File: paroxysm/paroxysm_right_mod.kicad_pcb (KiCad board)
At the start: 2 copper layers, 117.5 x 89.9 mm, 20 parts, among them SW10 SW_Push, SW11 SW_Push, SW12 SW_Push, SW14 SW_Push, SW15 SW_Push, SW16 SW_Push, SW17 SW_Push, SW18 SW_Push, SW20 SW_Push, SW21 SW_Push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

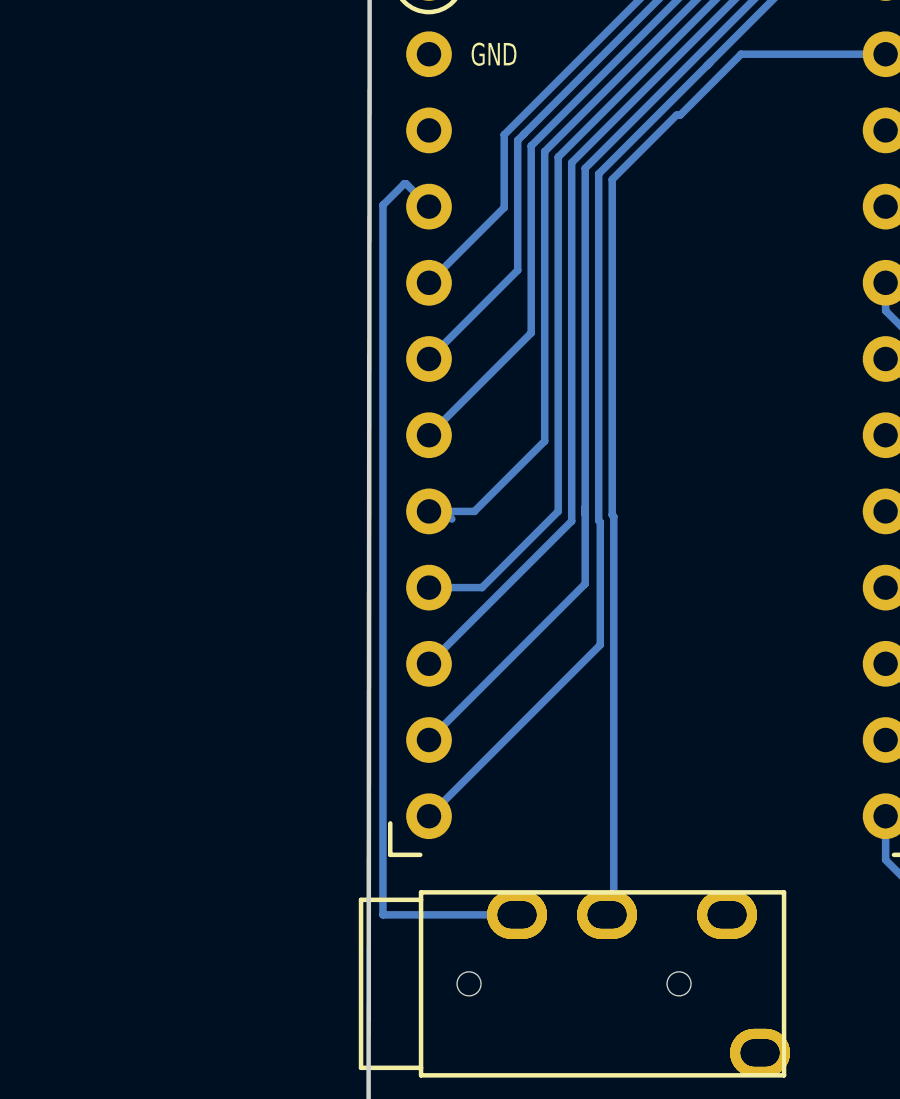
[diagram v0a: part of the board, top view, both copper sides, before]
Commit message: Update and corrected traces
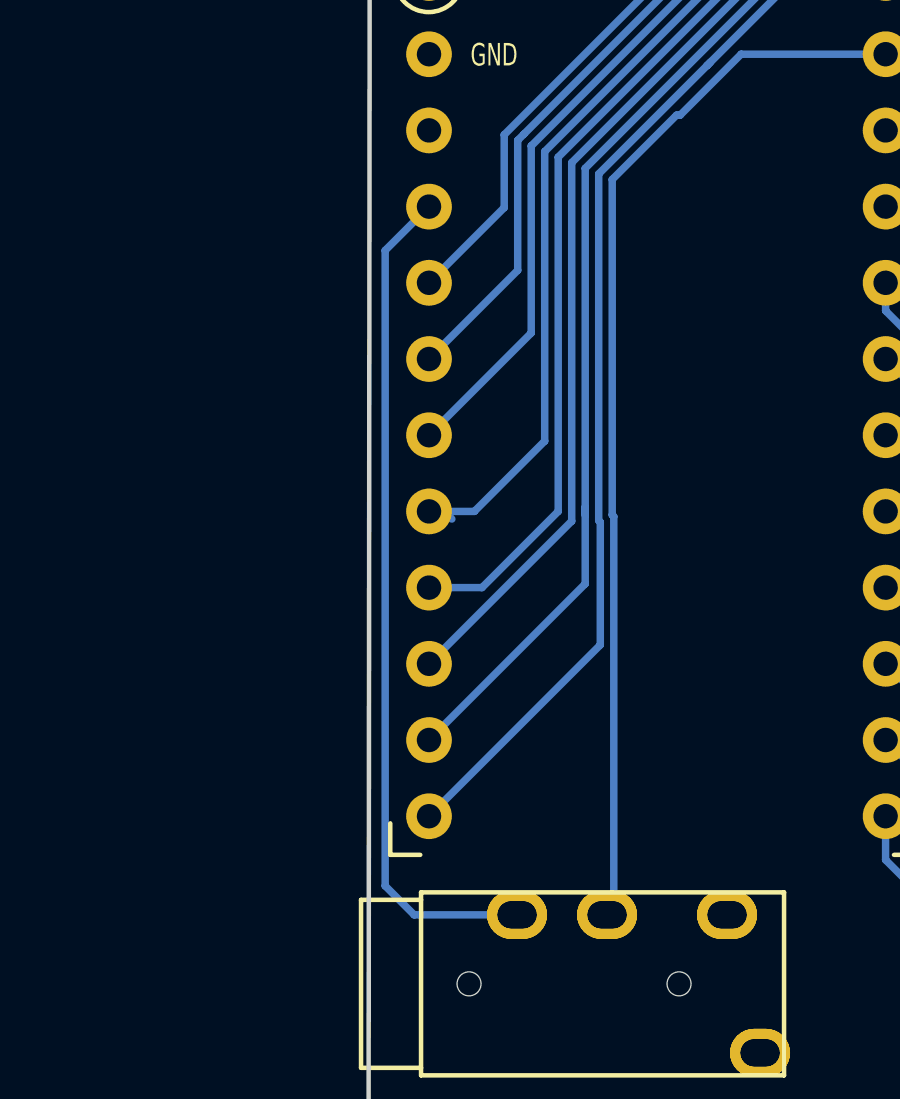
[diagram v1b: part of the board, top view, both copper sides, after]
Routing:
- net vcc: track 30.3 -> 28.0 mm
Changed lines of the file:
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@@
   (segment (start 81.28 62.738) (end 81.279998 62.737998) (width 0.25) (layer "B.Cu") (net 0))
   (segment (start 33.0314 57.658) (end 32.53523 57.658) (width 0.25) (layer "B.Cu") (net 1))
-  (segment (start 32.269401 59.436001) (end 32.208434 59.436001) (width 0.25) (layer "B.Cu") (net 3))
-  (segment (start 31.496 60.148435) (end 31.496 83.806) (width 0.25) (layer "B.Cu") (net 3))
-  (segment (start 32.208434 59.436001) (end 31.496 60.148435) (width 0.25) (layer "B.Cu") (net 3))
-  (segment (start 33.0314 60.198) (end 32.269401 59.436001) (width 0.25) (layer "B.Cu") (net 3))
-  (segment (start 31.496 83.806) (end 35.966 83.806) (width 0.25) (layer "B.Cu") (net 3))
+  (segment (start 35.966 83.806) (end 32.536 83.806) (width 0.25) (layer "B.Cu") (net 3))
+  (segment (start 31.57 82.84) (end 31.57 61.6594) (width 0.25) (layer "B.Cu") (net 3))
+  (segment (start 31.57 61.6594) (end 33.0314 60.198) (width 0.25) (layer "B.Cu") (net 3))
+  (segment (start 32.536 83.806) (end 31.57 82.84) (width 0.25) (layer "B.Cu") (net 3))
   (segment (start 43.434 55.118) (end 41.402 57.15) (width 0.25) (layer "B.Cu") (net 4))
   (segment (start 39.138039 59.294011) (end 39.138039 70.476801) (width 0.25) (layer "B.Cu") (net 4))
